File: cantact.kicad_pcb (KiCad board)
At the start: 2 copper layers, 36.1 x 59.9 mm, 40 parts, among them J1 Cantact, P2 SWD, P4 USB_C_Plug_USB2.0, U1 STM32F042C6T6, U3 MCP2551-I/SN, U4 XC6220B331MR-G, Y1 16 Mhz

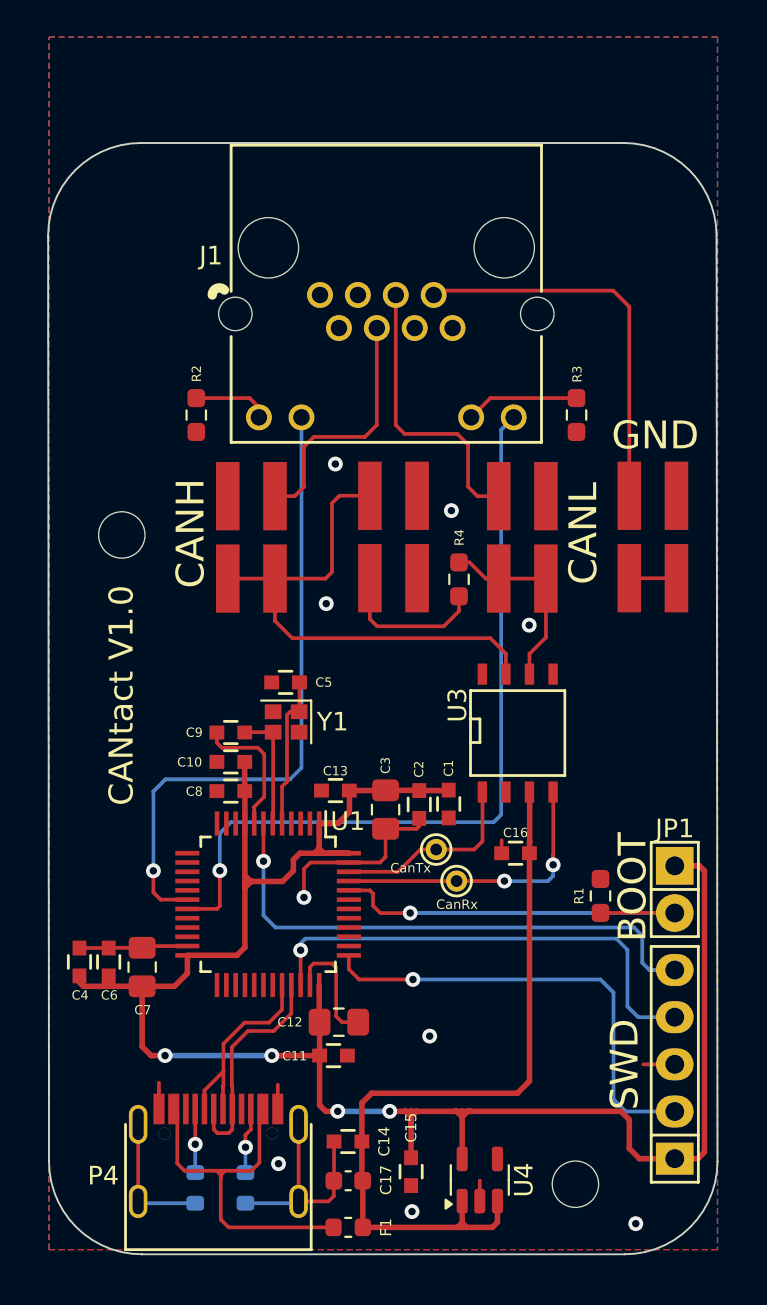
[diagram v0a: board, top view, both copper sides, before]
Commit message: refactor(hw): crystal position on PCB
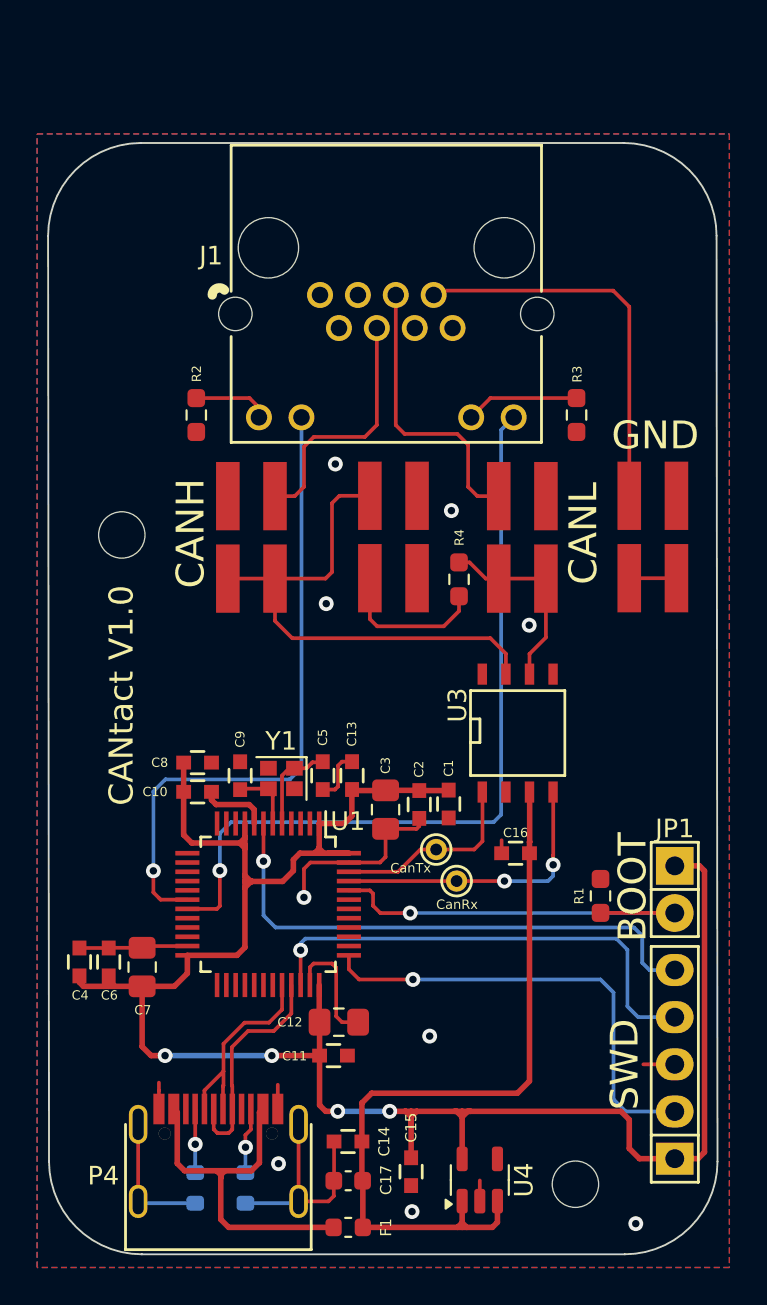
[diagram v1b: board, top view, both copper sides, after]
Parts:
- moved C5 5.41 mm to (139.0, 126.3), turned to -90 degrees
- moved Y1 3.05 mm to (136.8, 126.4)
- moved C10 2.41 mm to (132.3, 127.1), turned to 0 degrees
- moved C9 2.38 mm to (134.6, 126.3), turned to 90 degrees
- moved C8 2.36 mm to (132.3, 125.6), turned to 0 degrees
- moved C13 1.20 mm to (140.6, 126.3), turned to 90 degrees
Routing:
- net +3V3: track 109.1 -> 114.2 mm
- net Net-(U1-PF0-OSC_IN): track 8.27 -> 5.14 mm
- net Net-(U1-PF1-OSC_OUT): track 6.47 -> 3.53 mm
- net GND: track 57.7 -> 56.9 mm

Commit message: feat(hw): move differential pair of CANH and CANL
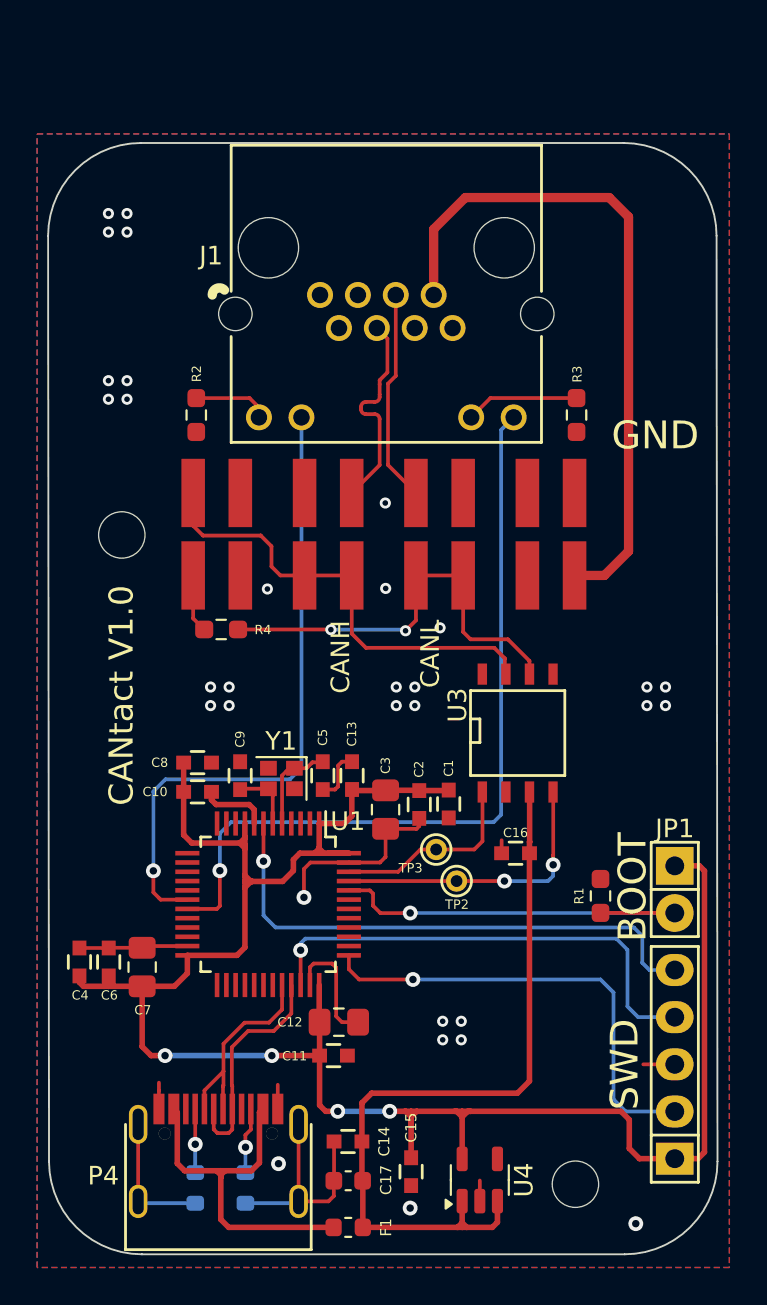
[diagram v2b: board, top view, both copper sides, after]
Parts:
- moved R4 13.1 mm to (133.6, 118.4), turned to 180 degrees
- moved JP2 9.52 mm to (133.3, 113.3)
- moved JP5 5.49 mm to (151.3, 113.3), turned to 180 degrees
- moved JP4 4.46 mm to (145.3, 113.3)
- moved JP3 4.14 mm to (139.3, 113.3)
- renumbered CanRx to TP2, CanTx to TP3
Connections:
- net /CANH1 renamed /CAN+
- net /CANL1 renamed /CAN-
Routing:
- net /GND1: track 21.2 -> 36.4 mm
- net Net-(JP4-Pin_1): track 10.6 -> 22.8 mm, vias 0 -> 2
- net Net-(JP2-Pin_1): track 8.30 -> 3.16 mm
- net /CAN-: track 15.5 -> 11.8 mm
- net Net-(JP2-Pin_2): track 28.2 -> 24.9 mm
- net GND: track 56.9 -> 54.4 mm, vias 9 -> 32
- net /CAN+: track 13.6 -> 11.5 mm

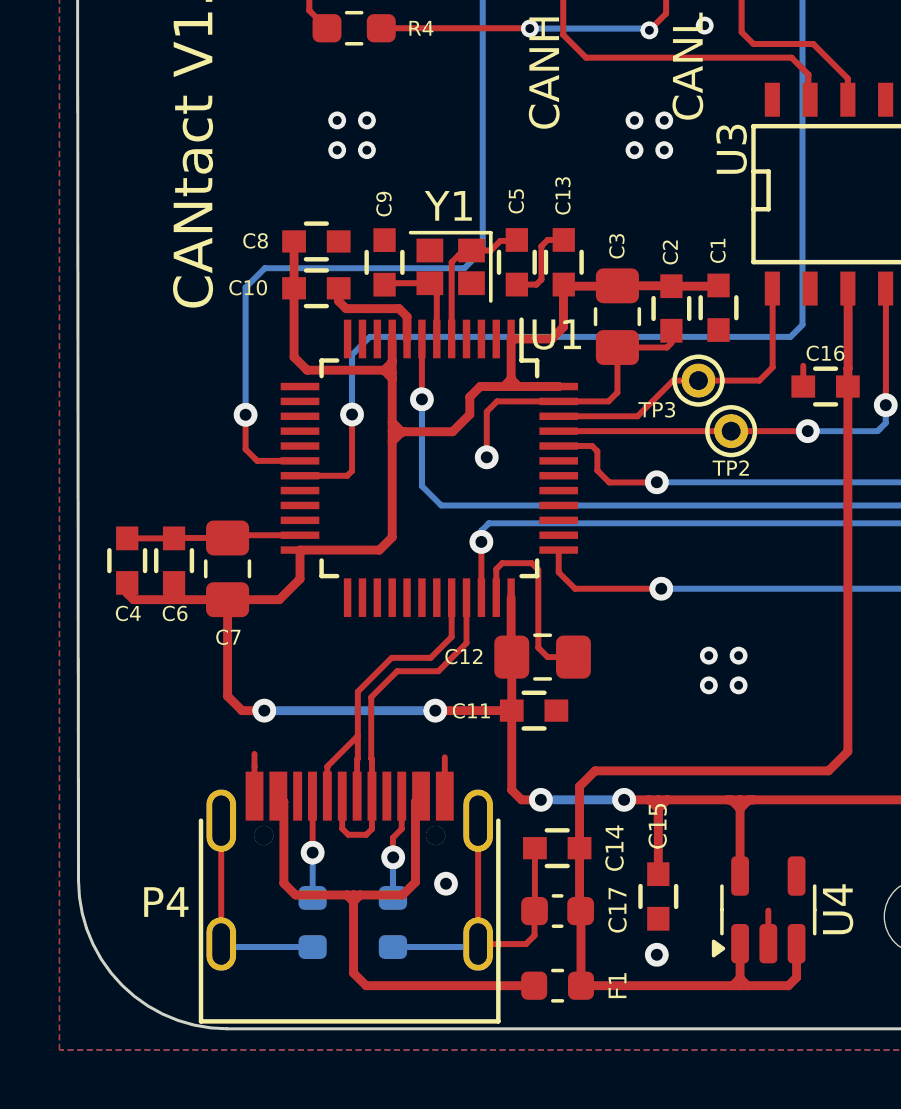
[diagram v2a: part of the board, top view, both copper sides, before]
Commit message: refactor: 3v net & change usb resistors to front layer
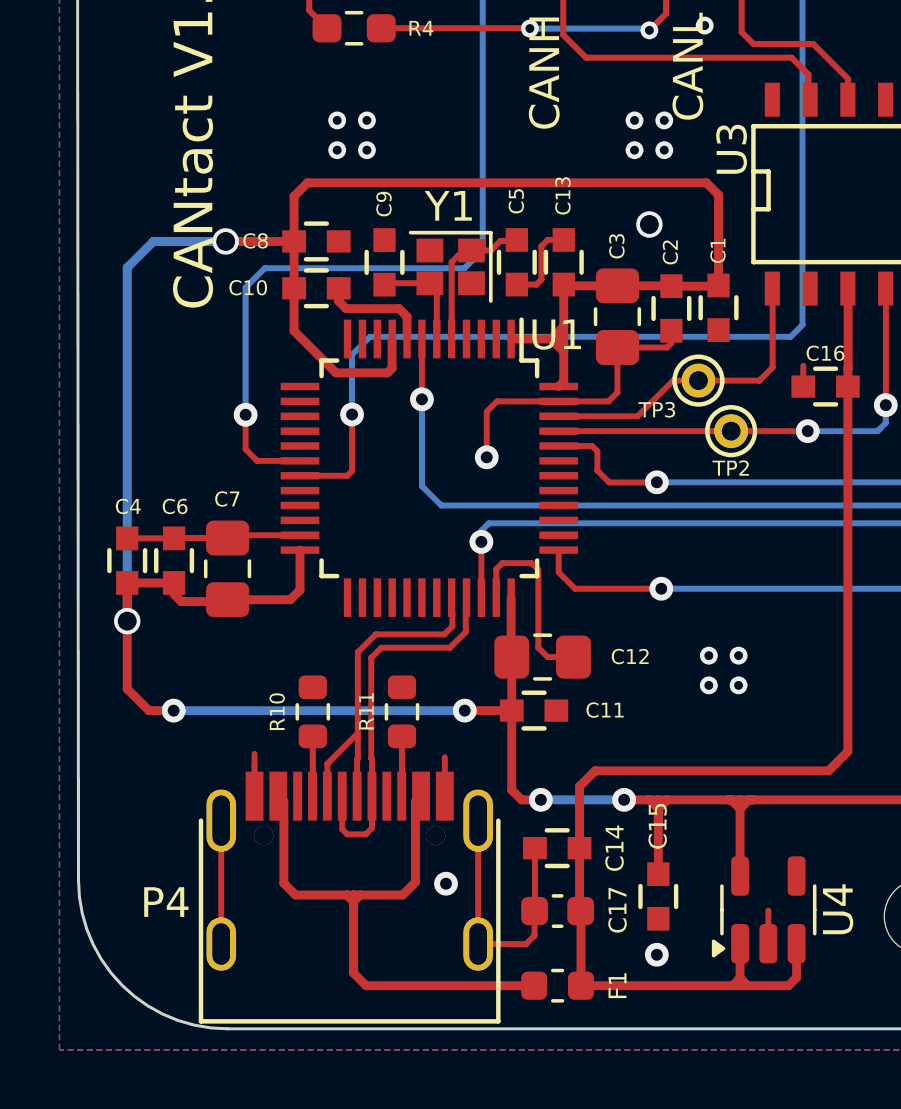
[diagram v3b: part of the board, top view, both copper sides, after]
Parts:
- R10, R11: moved to F.Cu
- moved R11 7.09 mm to (135.2, 141.4), turned to -90 degrees
- moved R10 7.09 mm to (132.2, 141.4), turned to -90 degrees
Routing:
- net +3V3: track 114.2 -> 135.2 mm, vias 4 -> 6
- net GND: track 54.4 -> 48.7 mm, vias 32 -> 33
- net Net-(P4-VCONN): track 3.56 -> 2.02 mm, vias 1 -> 0
- net Net-(P4-CC): track 3.43 -> 2.01 mm, vias 1 -> 0

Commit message: feat(hw): update pcb
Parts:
- moved R10 0.40 mm to (132.2, 141.0)
- moved R11 0.40 mm to (135.2, 141.0)
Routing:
- net GND: track 48.7 -> 53.4 mm, vias 33 -> 51
- net +3V3: track 135.2 -> 139.5 mm, vias 6 -> 5

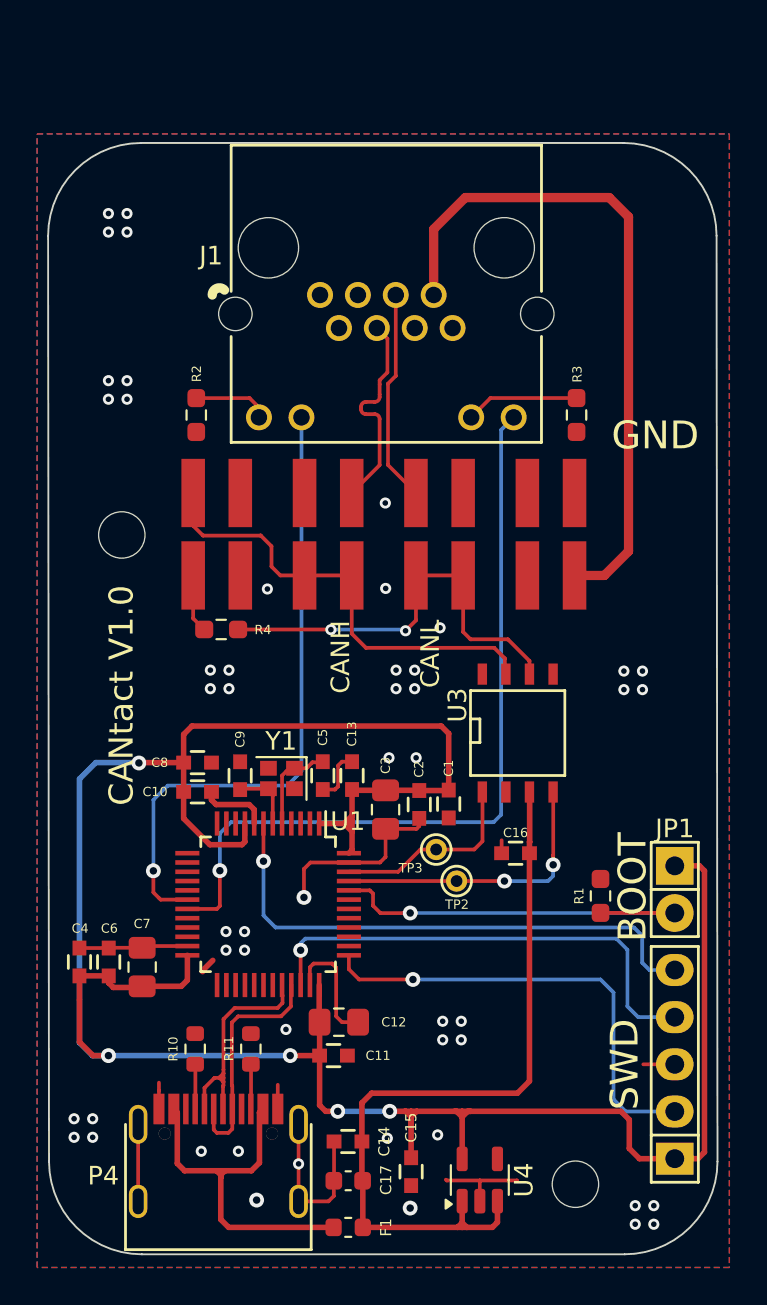
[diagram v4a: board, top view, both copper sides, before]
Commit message: feat(Hw):Update_Labels
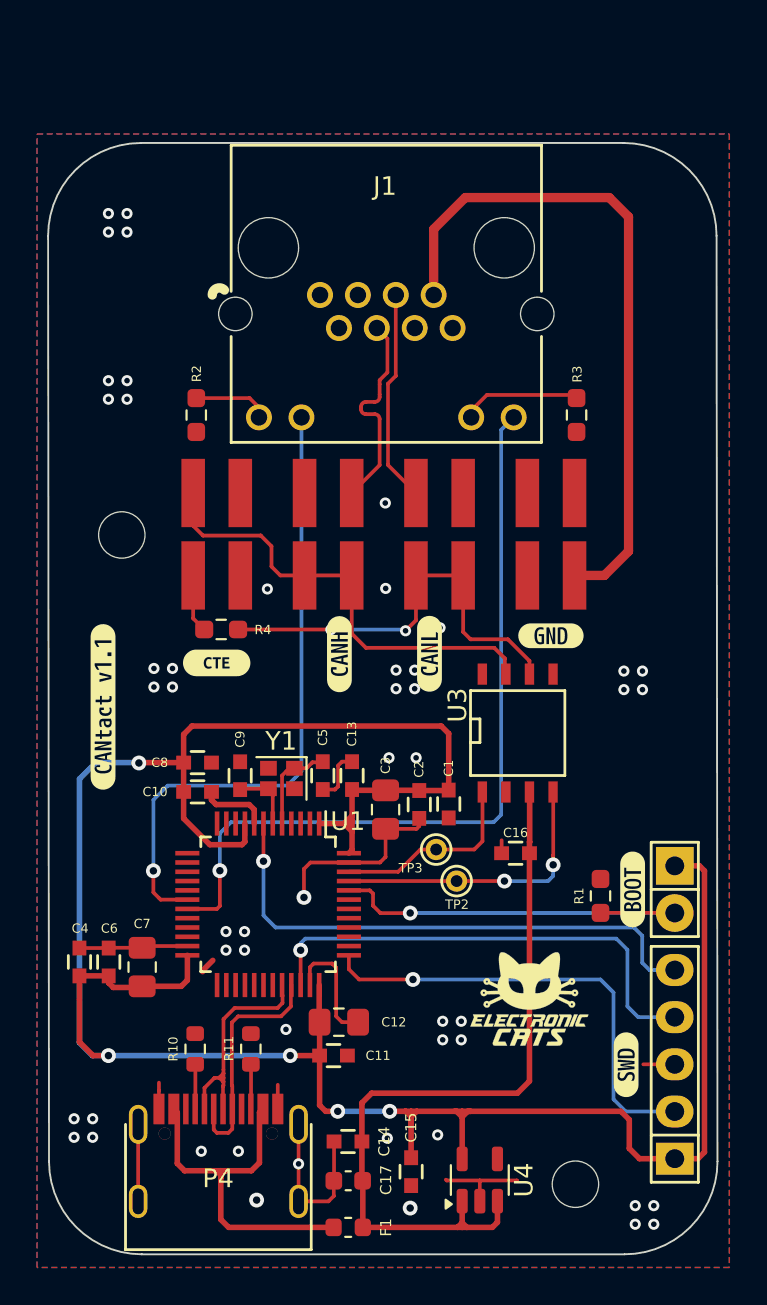
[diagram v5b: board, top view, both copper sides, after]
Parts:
- added G***: LOGO, Aesthetics:electronic_cats_logo_4x3, F.Cu at (150.2, 138.3)
- added G***: LOGO, Aesthetics:electronic_cats_logo_4x3, B.Cu at (142.6, 124.3)
- added kibuzzard-67FD8E9C: G***, kibuzzard-67FD8E9C, F.Cu at (155.4, 141.8)
- added kibuzzard-67FD8EBA: G***, kibuzzard-67FD8EBA, F.Cu at (155.7, 132.4)
- added kibuzzard-67FD8EE3: G***, kibuzzard-67FD8EE3, F.Cu at (151.3, 118.7)
- added kibuzzard-67FE7B2A: G***, kibuzzard-67FE7B2A, F.Cu at (139.9, 119.7)
- added kibuzzard-67FE7B45: G***, kibuzzard-67FE7B45, F.Cu at (144.8, 119.7)
- added kibuzzard-67FE8A9D: G***, kibuzzard-67FE8A9D, F.Cu at (127.2, 122.6)
- added kibuzzard-67FEBEE5: G***, kibuzzard-67FEBEE5, F.Cu at (133.3, 120.2)
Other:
- board text removed: "BOOT"
- board text removed: "CANH"
- board text removed: "CANL"
- board text removed: "CANtact V1.0"
- board text removed: "GND"
- board text removed: "SWD"

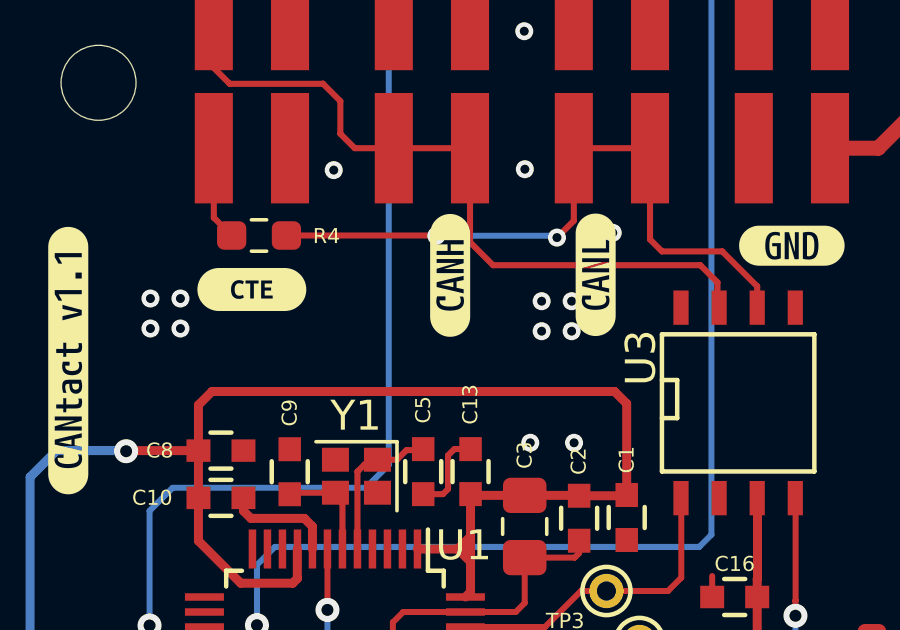
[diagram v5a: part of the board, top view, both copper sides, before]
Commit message: feat(Hw):Update_Labels
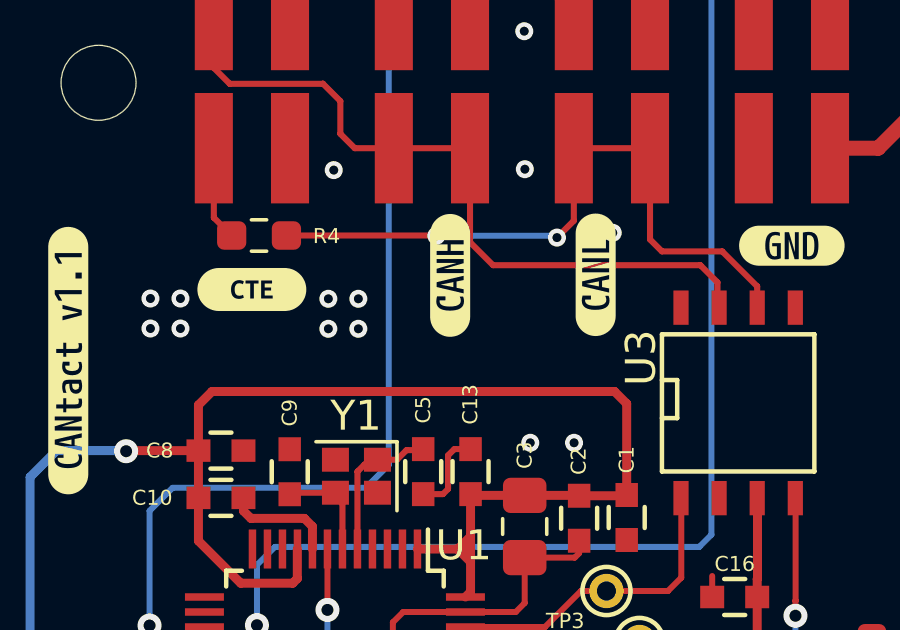
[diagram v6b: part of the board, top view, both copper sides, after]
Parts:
- added REF**: OSHW-Logo2_7.3x6mm_SilkScreen, Symbol:OSHW-Logo2_7.3x6mm_SilkScreen, B.Cu at (142.6, 133.7)
- added kibuzzard-67FE8A9D: G***, kibuzzard-67FE8A9D, B.Cu at (142.6, 126.5)
- moved G*** 1.59 mm to (142.5, 122.7)
